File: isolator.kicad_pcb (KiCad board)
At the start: 4 copper layers, 120 x 50 mm, 55 parts, among them J1 HOST, J2 ISO_PORT, Q1 2N7002, T1 750313638, U1 ADuM4165, U2 USBLC6-2SC6, U3 USBLC6-2SC6, U4 SN6505BDBV, U5 TLV76750DGNR, U6 TPS2553DBV, Y1 24M 8pF

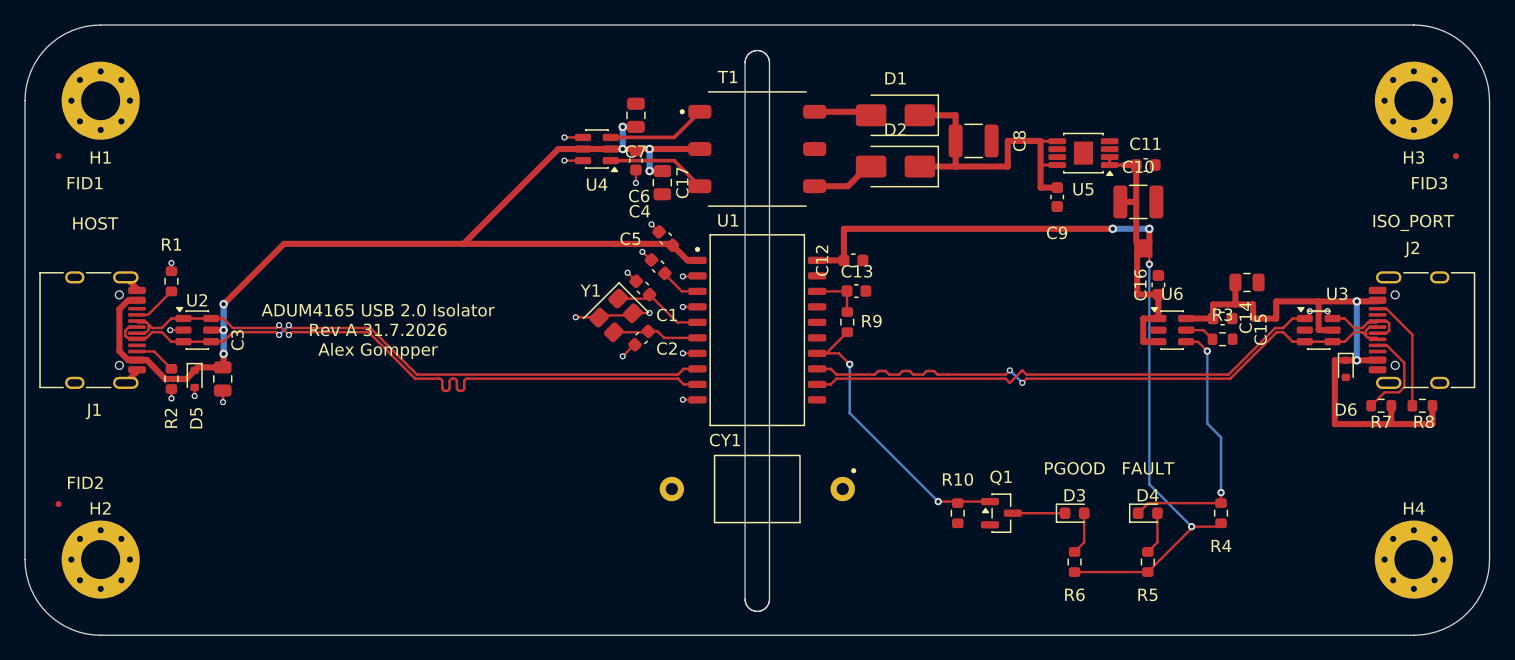
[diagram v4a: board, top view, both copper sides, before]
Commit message: wip: manual schematic re-layout and isolated-side board rework
Hand work done in the KiCad GUI, committed as a checkpoint. Not finished.

Schematic (nearly every symbol repositioned):
- VBUS_HOST, VDD1 and VDD2 are now driven by power symbols instead of
  local labels, so the nets lose their leading "/" and are global.
- NT2 deleted; /DCDC_RECT and /DCDC_RAW merge into one net.
- U3's two USBLC6 channels swapped (J2 D+ now enters on pin 3, D- on
  pin 1) and the J2-side labels removed, splitting /PORT_D+/- at the
  ESD part.
- D5 reversed: pin 2 now on VBUS_HOST, pin 1 on GND1.
- /RECT_A and /RECT_B swapped at T1's secondary (pins 4 and 6).
- /PG_LED_A and /PG_LED_K labels dropped.
- D3/D4 values annotated GREEN LED / RED LED.
- Mounting holes, fiducials and the PWR_FLAG bank parked off-sheet at
  negative x.

Board:
- NT2 footprint removed to match.
- 20 parts re-placed; C6/C7 and D1/D2 each swapped positions.
- Routing reworked with arcs (8 -> 101) and 23 more vias.
- Zone pad connection changed to reliefs-for-PTH-only and corner
  radius to 0.25 mm; the two via_dangling DRC exclusions dropped.

Co-Authored-By: Claude Opus 5 <noreply@anthropic.com>
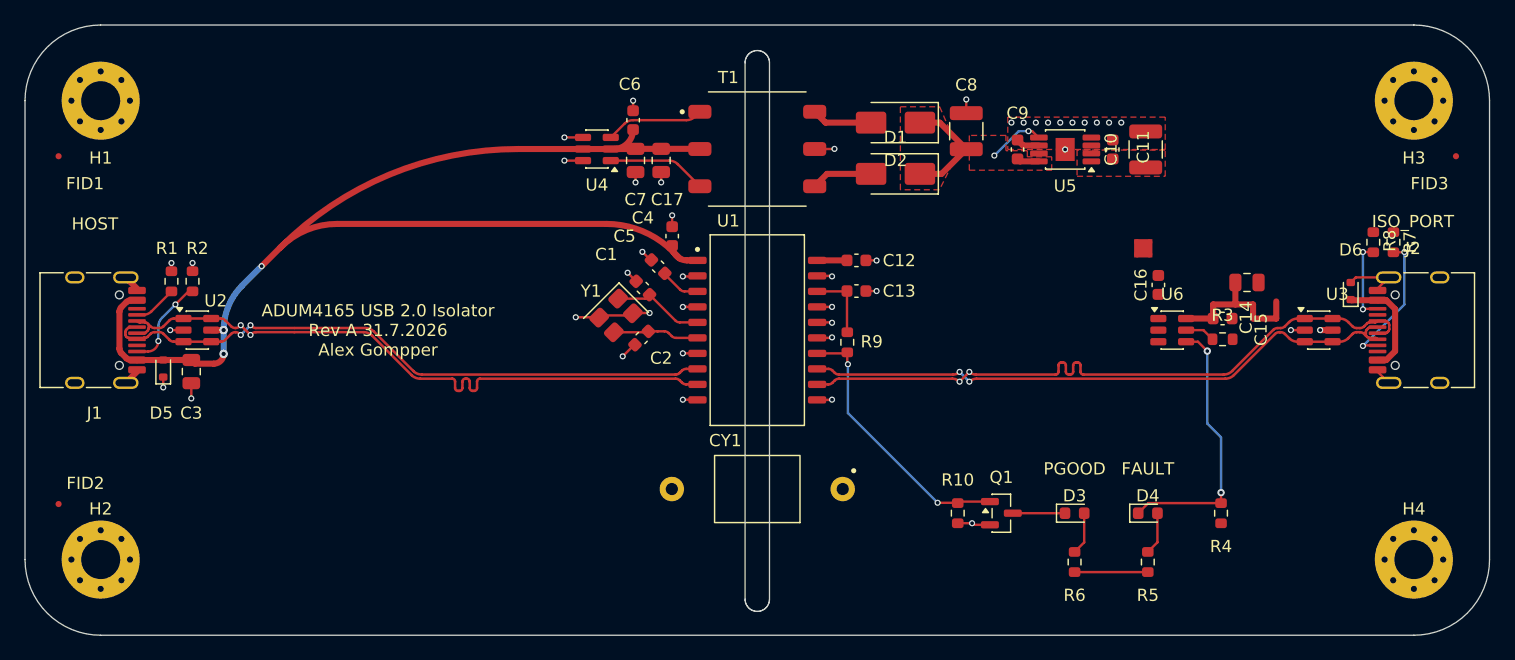
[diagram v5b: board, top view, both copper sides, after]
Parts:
- removed NT2: NetTie-2_SMD_Pad0.5mm, NetTie-2_SMD_Pad0.5mm
- C16: value C_0603_1608Metric -> 100n; footprint C_0603_1608Metric -> Capacitor_SMD:C_0603_1608Metric
- C17: value C_0805_2012Metric -> 4.7uF; footprint C_0805_2012Metric -> Capacitor_SMD:C_0805_2012Metric
- D3: value LED -> GREEN LED
- D4: value LED -> RED LED
- NT1: value NetTie-4_SMD_Pad0.5mm -> NetTie_4; footprint NetTie-4_SMD_Pad0.5mm -> NetTie:NetTie-4_SMD_Pad0.5mm
- NT3: value NetTie-2_SMD_Pad0.5mm -> NetTie_2; footprint NetTie-2_SMD_Pad0.5mm -> NetTie:NetTie-2_SMD_Pad0.5mm
- moved R8 14.0 mm to (197.3, 94.5), turned to -90 degrees
- moved R7 13.4 mm to (199.0, 94.5), turned to -90 degrees
- moved R2 8.19 mm to (100.6, 97.7), turned to 90 degrees
- moved D6 6.39 mm to (195.5, 98.5), turned to 90 degrees
- moved C9 5.08 mm to (168.2, 86.9), turned to 90 degrees
- moved D1 4.80 mm to (158.2, 88.9)
- moved C10 4.34 mm to (178.7, 86.9), turned to 90 degrees
- moved C7 3.70 mm to (136.9, 87.8), turned to -90 degrees
- moved D2 3.60 mm to (158.2, 84.7)
- moved C6 3.31 mm to (136.7, 84.5), turned to 90 degrees
- moved C11 2.99 mm to (176.0, 86.9), turned to 90 degrees
- moved D5 2.71 mm to (98.2, 104.8), turned to 90 degrees
- moved C3 2.64 mm to (100.5, 105.1)
- moved C17 1.82 mm to (139.0, 87.8)
- moved R9 1.65 mm to (154.2, 102.7)
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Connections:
- net /PG_LED_A renamed Net-(D3-A)
- net /PG_LED_K renamed Net-(D3-K)
- net /VDD1 renamed VDD1
- net /VDD2 renamed VDD2
- C17 pad 1: /VBUS_HOST -> VBUS_HOST
- C3 pad 1: /VBUS_HOST -> VBUS_HOST
- C4 pad 1: /VBUS_HOST -> VBUS_HOST
- C6 pad 1: /VBUS_HOST -> VBUS_HOST
- C7 pad 1: /VBUS_HOST -> VBUS_HOST
- C8 pad 1: /DCDC_RECT -> Net-(D1-K)
- C9 pad 1: /DCDC_RAW -> Net-(D1-K)
- D1 pad 1: /DCDC_RECT -> Net-(D1-K)
- D2 pad 1: /DCDC_RECT -> Net-(D1-K)
- D5 pad 1: /VBUS_HOST -> GND1
- D5 pad 2: GND1 -> VBUS_HOST
- J1 pad A4: /VBUS_HOST -> VBUS_HOST
- J1 pad A9: /VBUS_HOST -> VBUS_HOST
- J1 pad B4: /VBUS_HOST -> VBUS_HOST
- J1 pad B9: /VBUS_HOST -> VBUS_HOST
- J2 pad A6: /PORT_D+ -> Net-(J2-D+-PadA6)
- J2 pad A7: /PORT_D- -> Net-(J2-D--PadA7)
- J2 pad B6: /PORT_D+ -> Net-(J2-D+-PadA6)
- J2 pad B7: /PORT_D- -> Net-(J2-D--PadA7)
- T1 pad 2: /VBUS_HOST -> VBUS_HOST
- T1 pad 4: /RECT_B -> /RECT_A
- T1 pad 6: /RECT_A -> /RECT_B
- U1 pad 1: /VBUS_HOST -> VBUS_HOST
- U2 pad 5: /VBUS_HOST -> VBUS_HOST
- U3 pad 1: /PORT_D+ -> Net-(J2-D--PadA7)
- U3 pad 3: /PORT_D- -> Net-(J2-D+-PadA6)
- U3 pad 4: /PORT_D- -> /PORT_D+
- U3 pad 6: /PORT_D+ -> /PORT_D-
- U4 pad 2: /VBUS_HOST -> VBUS_HOST
- U4 pad 5: /VBUS_HOST -> VBUS_HOST
- U5 pad 5: /DCDC_RAW -> Net-(D1-K)
- U5 pad 8: /DCDC_RAW -> Net-(D1-K)
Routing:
- net VBUS_HOST: track 0.00 -> 102.7 mm, vias 0 -> 3
- net /VBUS_HOST: track 90.7 -> 0.00 mm, vias 7 -> 0
- net /ISO_5V_IND: track 37.5 -> 6.00 mm, vias 2 -> 0
- net /ISO_5V_VBUS2: track 30.9 -> 2.45 mm, vias 2 -> 0
- net /PORT_VBUS_J2: track 38.6 -> 12.5 mm, vias 2 -> 1
- net GND2: track 0.00 -> 22.3 mm, vias 0 -> 22
- net /DCDC_RECT: track 17.2 -> 0.00 mm
- net Net-(D1-K): track 0.00 -> 15.9 mm, vias 0 -> 2
- net /ISO_5V_SW: track 11.4 -> 0.00 mm
- net /ISO_5V: track 10.5 -> 0.00 mm
- net /DCDC_RAW: track 8.80 -> 0.00 mm
- net Net-(J1-CC2): track 3.42 -> 7.58 mm, vias 0 -> 2
- net /PORT_CC1: track 8.13 -> 11.2 mm, vias 0 -> 2
- net /PORT_CC2: track 9.55 -> 6.78 mm, vias 0 -> 2
- net GND1: track 25.1 -> 27.1 mm, vias 18 -> 20
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- added copper zone on F.Cu, net /ISO_5V
- added copper zone on F.Cu, net GND2
- added copper zone on F.Cu, net Net-(D1-K)
